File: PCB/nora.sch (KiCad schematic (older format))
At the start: 218 parts, among them J1 USB_C_Receptacle_USB2.0, J2 Conn_01x04, J3 Conn_01x02, J5 Conn_02x03_Odd_Even, U1 ATmega32U4-MU, U2 24LC64, U4 Pico, Y1 16MHz

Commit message: WIP 怪しそうなところを配線中
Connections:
- net row8: now also U1.30 (PB6); no longer U1.32 (PC7)
- net row9: now also U1.32 (PC7); no longer U1.30 (PB6)
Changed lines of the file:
@@
 Text GLabel 15325 2575 2    50   Input ~ 0
 row1
-Text GLabel 15325 2875 2    50   Input ~ 0
+Text GLabel 15325 2475 2    50   Input ~ 0
 row8
 Text GLabel 15325 1875 2    50   Input ~ 0
 row5
-Text GLabel 15325 2475 2    50   Input ~ 0
+Text GLabel 15325 2875 2    50   Input ~ 0
 row9
 Text GLabel 15325 2275 2    50   Input ~ 0

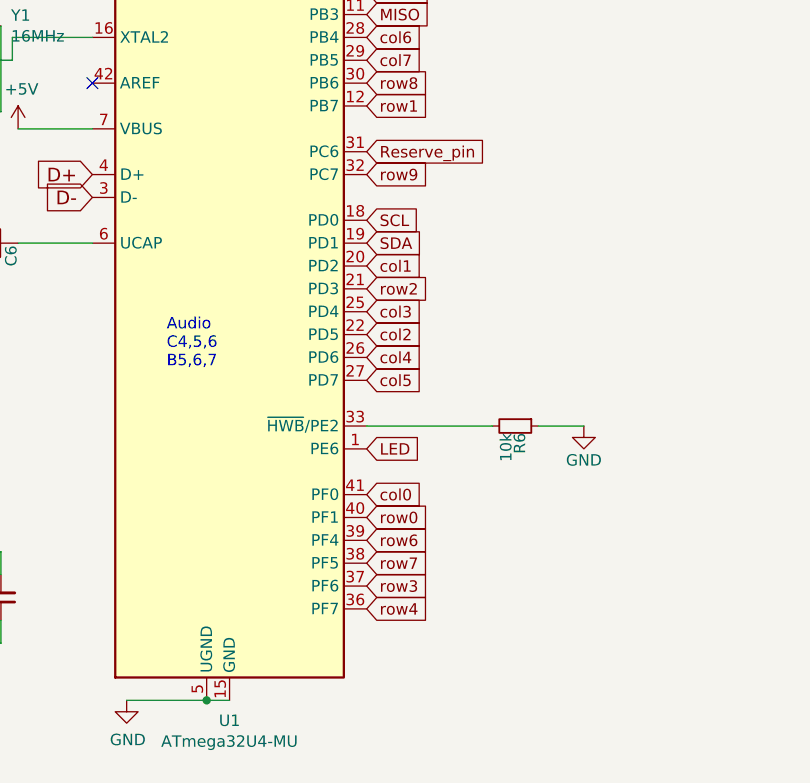
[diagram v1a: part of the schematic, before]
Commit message: ソケット化と、関連するパーツの配置と配線に目処が立つ#1
FULL hotswap socket support
Fixes #1
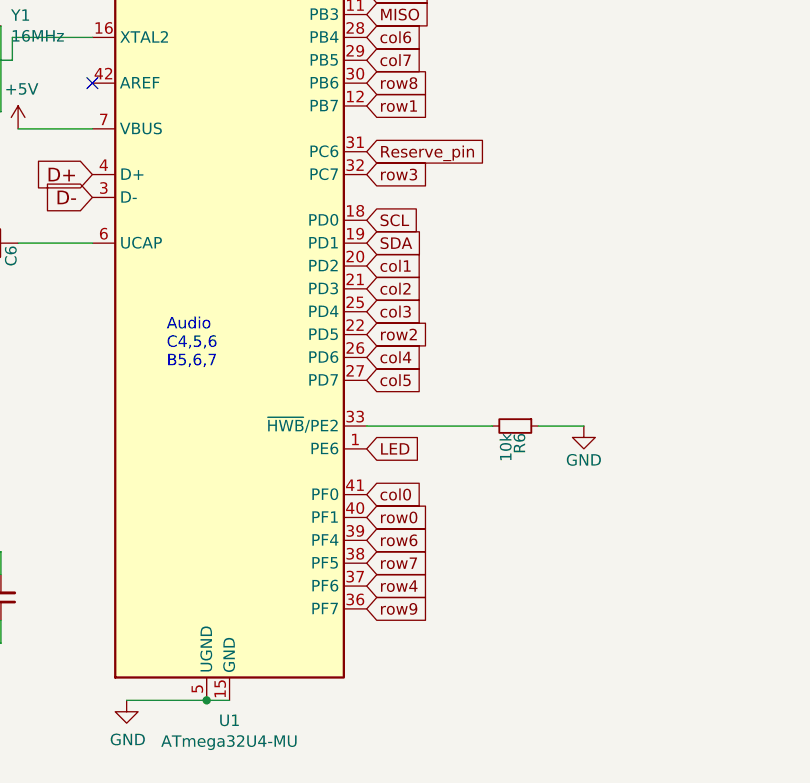
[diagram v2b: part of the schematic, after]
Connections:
- net col2: now also U1.21 (PD3); no longer U1.22 (PD5)
- net row2: now also U1.22 (PD5); no longer U1.21 (PD3)
- net row3: now also U1.32 (PC7); no longer U1.37 (PF6)
- net row4: now also U1.37 (PF6); no longer U1.36 (PF7)
- net row9: now also U1.36 (PF7); no longer U1.32 (PC7)
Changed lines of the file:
@@
 Text GLabel 15325 4375 2    50   Input ~ 0
 row0
+Text GLabel 15325 2875 2    50   Input ~ 0
+row3
 Text GLabel 15325 4675 2    50   Input ~ 0
-row3
-Text GLabel 15325 4775 2    50   Input ~ 0
 row4
 Text GLabel 15325 4575 2    50   Input ~ 0
@@
 Text GLabel 15325 1875 2    50   Input ~ 0
 row5
-Text GLabel 15325 2875 2    50   Input ~ 0
+Text GLabel 15325 4775 2    50   Input ~ 0
 row9
 Text GLabel 15325 2275 2    50   Input ~ 0
@@
 Text GLabel 15325 1975 2    50   Input ~ 0
 SCK
+Text GLabel 15325 3375 2    50   Input ~ 0
+col2
 Text GLabel 15325 3575 2    50   Input ~ 0
-col2
-Text GLabel 15325 3375 2    50   Input ~ 0
 row2
 Wire Wire Line

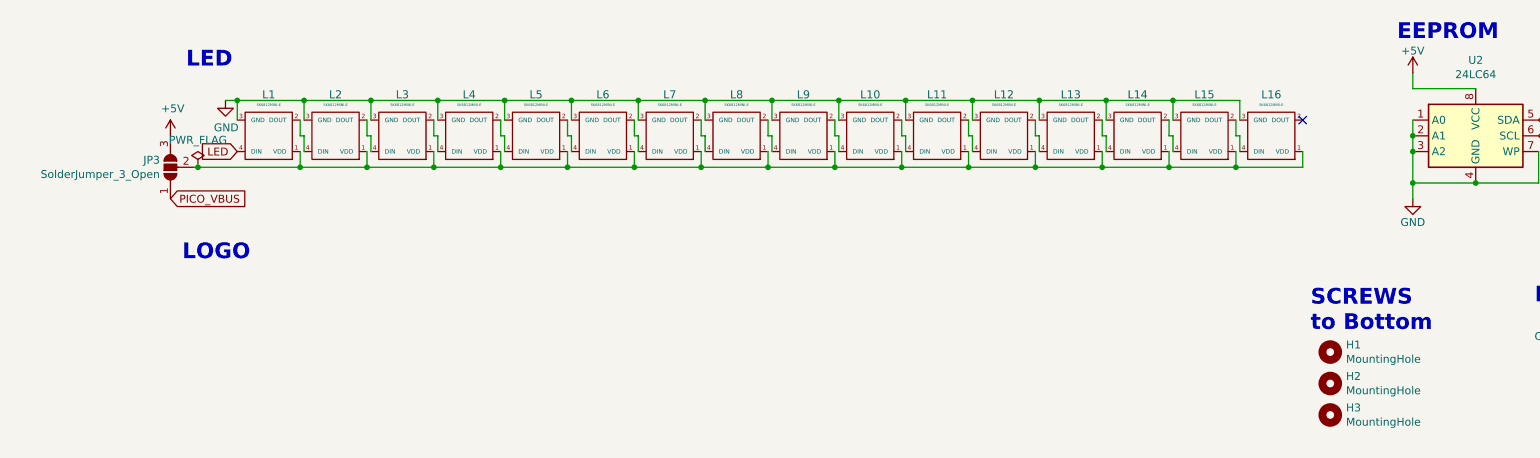
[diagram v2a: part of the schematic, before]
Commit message: WIP 回路図へLED追加。とりあえずPCBへ配置
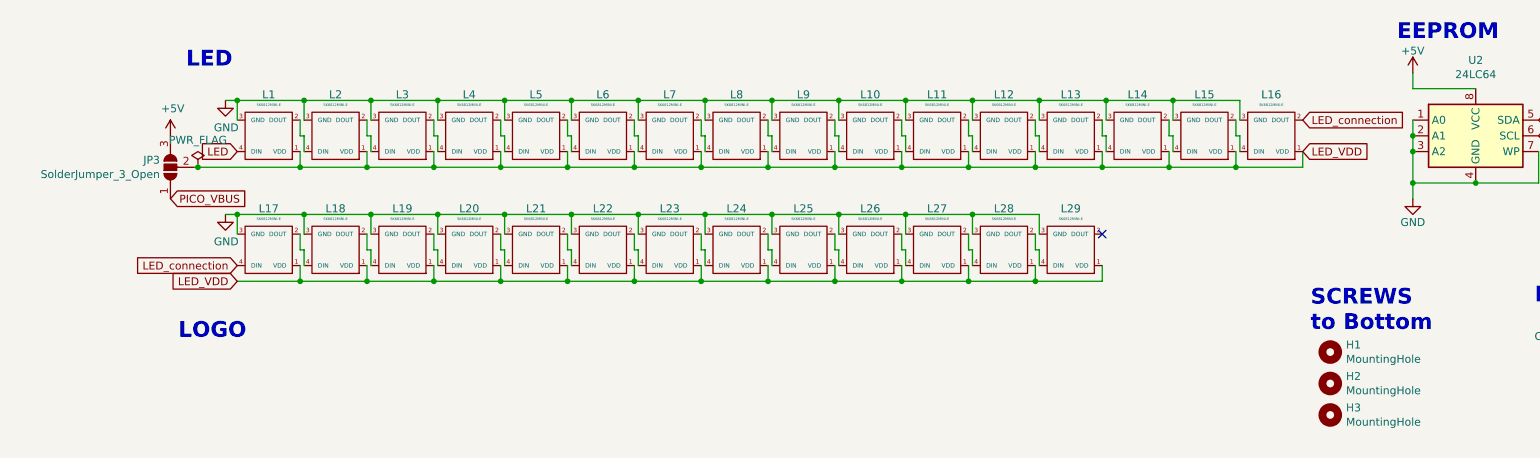
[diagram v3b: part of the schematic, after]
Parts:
- added L17, L18, L19, L20, L21, L22, L23, L24, L25, L26, L27, L28, L29: SK6812MINI-E, Jones.local:YS-SK6812MINI-E, symbol kbd:SK6812MINI-E
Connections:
- net GND: now also L17.3 (GND), L18.3 (GND), L19.3 (GND), L20.3 (GND), L21.3 (GND), L22.3 (GND), L23.3 (GND), L24.3 (GND), L25.3 (GND), L26.3 (GND), L27.3 (GND), L28.3 (GND), L29.3 (GND)
- net LED_VDD: now reaches JP3.2 (C), L1.1 (VDD), L10.1 (VDD), L11.1 (VDD), L12.1 (VDD), L13.1 (VDD), L14.1 (VDD), L15.1 (VDD), L16.1 (VDD), L2.1 (VDD), L3.1 (VDD), L4.1 (VDD), L5.1 (VDD), L6.1 (VDD), L7.1 (VDD), L8.1 (VDD), L9.1 (VDD)
- net LED_VDD: now also L17.1 (VDD), L18.1 (VDD), L19.1 (VDD), L20.1 (VDD), L21.1 (VDD), L22.1 (VDD), L23.1 (VDD), L24.1 (VDD), L25.1 (VDD), L26.1 (VDD), L27.1 (VDD), L28.1 (VDD), L29.1 (VDD)
- net LED_connection: now reaches L16.2 (DOUT)
- net LED_connection: now also L17.4 (DIN)
- new net: L18.2 (DOUT), L19.4 (DIN)
- new net: L17.2 (DOUT), L18.4 (DIN)
- new net: L20.2 (DOUT), L21.4 (DIN)
- new net: L19.2 (DOUT), L20.4 (DIN)
- new net: L22.2 (DOUT), L23.4 (DIN)
- new net: L21.2 (DOUT), L22.4 (DIN)
- new net: L24.2 (DOUT), L25.4 (DIN)
- new net: L23.2 (DOUT), L24.4 (DIN)
- new net: L26.2 (DOUT), L27.4 (DIN)
- new net: L25.2 (DOUT), L26.4 (DIN)
- new net: L28.2 (DOUT), L29.4 (DIN)
- new net: L27.2 (DOUT), L28.4 (DIN)

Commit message: WIP 配線
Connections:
- net col2: now also U1.25 (PD4); no longer U1.21 (PD3)
- net col3: now also U1.21 (PD3); no longer U1.25 (PD4)
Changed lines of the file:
@@
 Text GLabel 15325 3275 2    50   Input ~ 0
 col1
-Text GLabel 15325 3475 2    50   Input ~ 0
+Text GLabel 15325 3375 2    50   Input ~ 0
 col3
 Text GLabel 15325 3775 2    50   Input ~ 0
@@
 Text GLabel 15325 1975 2    50   Input ~ 0
 SCK
-Text GLabel 15325 3375 2    50   Input ~ 0
+Text GLabel 15325 3475 2    50   Input ~ 0
 col2
 Text GLabel 15325 3575 2    50   Input ~ 0

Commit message: ロゴ配置完了, Renew logo on PCB #11
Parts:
- D1, D11, D12, D13, D14, D15, D16, D17, D18, D19, D2, D20, D21, D22, D23, D25, D26, D27, D28, D29, D3, D30, D31, D32, D33, D35, D36, D37, D38, D39, D4, D40, D41, D42, D43, D45, D46, D47, D48, D49, D5, D50, D51, D52, D53, D54, D55, D56, D57, D58, D59, D6, D60, D61, D62, D63, D64, D65, D66, D67, D68, D69, D7, D70, D71, D72, D73, D74, D75, D76, D77, D78, D79, D8, D9: footprint locallib:D_SOD-123_Refelence@Left -> locallib:D_SOD-123-Pretty_No_Reference
